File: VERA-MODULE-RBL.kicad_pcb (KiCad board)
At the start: 4 copper layers, 143 x 162.5 mm, 177 parts, among them J1 CONN_SMD_02x08_Odd_Even_2.54mm, J2 ICD15S13E4GX00LF, J3 CONN_DM3AT-SF-PEJM5, J4 DX07S016JA1R1500, J5 PJ-002AH-SMT-TR, Q1 MOSFET-BSS138-SOT-23, Q2 MOSFET-BSS138-SOT-23, Q3 BC817,SOT-23, Q4 BC817,SOT-23, Q5 MOSFET-BSS138-SOT-23, SW1 SPST2P, SW2 SPST_SWITCH_SMD_4P,4.1x5.4mm, U1 TXS0108EPW, U10 W25Q16JVSNIQ, U11 WM8524CGEDT, U12 USBCH340T, U13 AMS1117-3.3, U14 AMS1117-1.5, U15 L7805, U16 TXS0108EPW, U17 MAX40200AUK, U2 ICE40UP5K-SG48ITR, U3 TXS0108EPW, U4 TXS0108EPW, U5 IC74HC00, U6 TXS0108EPW, U7 ESP32-PICO-D4, U8 74CBTLV3126PW,118, U9 IC74HC00, X1 SG-5032CAN, Y1 12MHzC

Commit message: Updated
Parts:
- C11, C26, C27, C29, C32, C33, C35, R42, R6, R66, U16, U3, U8: moved to B.Cu
- C2, R2, R64, U1, U6: moved to F.Cu
- X1: value SG-5032CAN -> ECS-2033-250-BN; footprint Oscillator:Oscillator_SMD_SeikoEpson_SG8002LB-4Pin_5.0x3.2mm -> RetroBitLab:OSC_ECS-2033-250-BN
- moved C26 125.3 mm to (256.4, 50.5)
- moved R41 121.0 mm to (273.2, 72.2), turned to 90 degrees
- moved C28 118.4 mm to (259.4, 61.5), turned to 90 degrees
- moved C27 110.8 mm to (250.6, 50.9), turned to 180 degrees
- moved R37 110.7 mm to (263.2, 72.1), turned to 90 degrees
- moved C52 110.2 mm to (259.4, 56.2), turned to 270 degrees
- moved R39 108.1 mm to (268.1, 72.2), turned to 90 degrees
- moved R40 106.6 mm to (270.6, 72.2), turned to 90 degrees
- moved R49 102.8 mm to (165.8, 77.0), turned to 180 degrees
- moved R38 100.7 mm to (265.6, 72.1), turned to 90 degrees
- moved U8 97.8 mm to (250.4, 57.9), turned to 90 degrees
- moved C29 94.1 mm to (239.4, 54.0)
- moved R42 89.4 mm to (245.6, 54.9), turned to 180 degrees
- moved R44 88.5 mm to (235.4, 67.6), turned to 180 degrees
- moved C34 87.8 mm to (232.0, 84.9)
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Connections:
- C1 pad 2: +3V3 -> 3V3
- C10 pad 2: +5V -> 3V3
- C11 pad 2: +3V3 -> 3V3
- C12 pad 2: +5V -> 5V
- C2 pad 2: +5V -> 3V3
- C55 pad 2: +3V3 -> 5V
- C56 pad 2: +5V -> 5V
- C57 pad 2: +3V3 -> 5V
- C58 pad 2: +5V -> 5V
- C9 pad 2: +3V3 -> 3V3
- J2 pad 9: +5V -> 5V
- LD2 pad 2: +3V3 -> 3V3
- R2 pad 1: +3V3 -> 3V3
- R6 pad 1: +3V3 -> 3V3
- R64 pad 1: +3V3 -> 3V3
- R66 pad 1: +3V3 -> 3V3
- R7 pad 1: +3V3 -> 3V3
- U1 pad 1: mD2 -> mRD4
- U1 pad 12: ~S4 -> A12
- U1 pad 13: A3 -> A9
- U1 pad 14: A2 -> A8
- U1 pad 15: A1 -> A7
- U1 pad 16: A0 -> A6
- U1 pad 17: D4 -> A5
- U1 pad 18: D5 -> A4
- U1 pad 19: +5V -> 5V
- U1 pad 2: +3V3 -> 3V3
- U1 pad 20: D2 -> RD4
- U1 pad 3: mD5 -> mA4
- U1 pad 4: mD4 -> mA5
- U1 pad 5: mA0 -> mA6
- U1 pad 6: mA1 -> mA7
- U1 pad 7: mA2 -> mA8
- U1 pad 8: mA3 -> mA9
- U1 pad 9: ~mS4 -> mA12
- U16 pad 1: ~mHALT -> ~FPGA_RESET
- U16 pad 12: ~WE -> D1
- U16 pad 13: ~RE -> D0
- U16 pad 14: ~MPD -> D6
- U16 pad 15: ~D1XX -> ~S5
- U16 pad 16: A15 -> RD5
- U16 pad 17: A14 -> ~CCTL
- U16 pad 18: A13 -> ~EXSEL
- U16 pad 19: +5V -> 5V
- U16 pad 2: +3V3 -> 3V3
- U16 pad 20: ~HALT -> ~RST
- U16 pad 3: mA13 -> ~mEXSEL
- U16 pad 4: mA14 -> ~mCCTL
- U16 pad 5: mA15 -> mRD5
- U16 pad 6: ~mD1XX -> ~mS5
- U16 pad 7: ~mMPD -> mD6
- U16 pad 8: ~mRE -> mD0
- U16 pad 9: ~mWE -> mD1
- U3 pad 1: mRD4 -> mD2
- U3 pad 12: A12 -> ~S4
- U3 pad 13: A9 -> A3
- U3 pad 14: A8 -> A2
- U3 pad 15: A7 -> A1
- U3 pad 16: A6 -> A0
- U3 pad 17: A5 -> D4
- U3 pad 18: A4 -> D5
- U3 pad 19: +5V -> 5V
- U3 pad 2: +3V3 -> 3V3
- U3 pad 20: RD4 -> D2
- U3 pad 3: mA4 -> mD5
- U3 pad 4: mA5 -> mD4
- U3 pad 5: mA6 -> mA0
- U3 pad 6: mA7 -> mA1
- U3 pad 7: mA8 -> mA2
- U3 pad 8: mA9 -> mA3
- U3 pad 9: mA12 -> ~mS4
- U4 pad 1: mD3 -> ~mHALT
- U4 pad 12: ~IRQ -> ~WE
- U4 pad 13: RSRVD -> ~RE
- U4 pad 14: PHI2 -> ~MPD
- U4 pad 15: R~W -> ~D1XX
- U4 pad 16: A10 -> A15
- U4 pad 17: A11 -> A14
- U4 pad 18: D7 -> A13
- U4 pad 19: +5V -> 5V
- U4 pad 2: +3V3 -> 3V3
- U4 pad 20: D3 -> ~HALT
- U4 pad 3: mD7 -> mA13
- U4 pad 4: mA11 -> mA14
- U4 pad 5: mA10 -> mA15
- U4 pad 6: mR~W -> ~mD1XX
- U4 pad 7: mPHI2 -> ~mMPD
- U4 pad 8: mRSRVD -> ~mRE
- U4 pad 9: ~mVIRQ -> ~mWE
- U6 pad 1: ~FPGA_RESET -> mD3
- U6 pad 12: D1 -> ~IRQ
- U6 pad 13: D0 -> RSRVD
- U6 pad 14: D6 -> PHI2
- U6 pad 15: ~S5 -> R~W
- U6 pad 16: RD5 -> A10
- U6 pad 17: ~CCTL -> A11
- U6 pad 18: ~EXSEL -> D7
- U6 pad 19: +5V -> 5V
- U6 pad 2: +3V3 -> 3V3
- U6 pad 20: ~RST -> D3
- U6 pad 3: ~mEXSEL -> mD7
- U6 pad 4: ~mCCTL -> mA11
- U6 pad 5: mRD5 -> mA10
- U6 pad 6: ~mS5 -> mR~W
- U6 pad 7: mD6 -> mPHI2
- U6 pad 8: mD0 -> mRSRVD
- U6 pad 9: mD1 -> ~mVIRQ
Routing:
- net 5V: track 41.9 -> 617.0 mm, vias 3 -> 19
- net GND: track 93.6 -> 406.9 mm, vias 26 -> 92
- net 3V3: track 88.7 -> 399.5 mm, vias 14 -> 76
- net AUDIOL: track 2.23 -> 217.3 mm, vias 0 -> 3
- net ~mD1XX: track 0.00 -> 194.5 mm, vias 0 -> 11
- net ~D1XX: track 27.9 -> 217.7 mm, vias 2 -> 9
- net AUDIOR: track 2.09 -> 182.1 mm, vias 0 -> 6
- net TXB_EN: track 13.2 -> 191.9 mm, vias 0 -> 10
- net mD0: track 2.04 -> 180.8 mm, vias 1 -> 7
- net mA3: track 11.5 -> 181.3 mm, vias 0 -> 10
- net mA1: track 10.6 -> 178.3 mm, vias 0 -> 9
- net mD5: track 0.00 -> 161.0 mm, vias 0 -> 7
- net mD7: track 0.00 -> 160.7 mm, vias 0 -> 10
- net mD4: track 0.00 -> 160.5 mm, vias 0 -> 6
- net mA7: track 0.00 -> 159.5 mm, vias 0 -> 5
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- added copper zone on F.Cu, net 3V3
- added copper zone on POWER, net 3V3
- added copper zone on B.Cu, net GND
- added copper zone on F.Cu, net GND
- added copper zone on GND, net GND
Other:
- board text added: "EXTERNAL VIDEO CONNECTOR"
- board text added: "VERA READY"

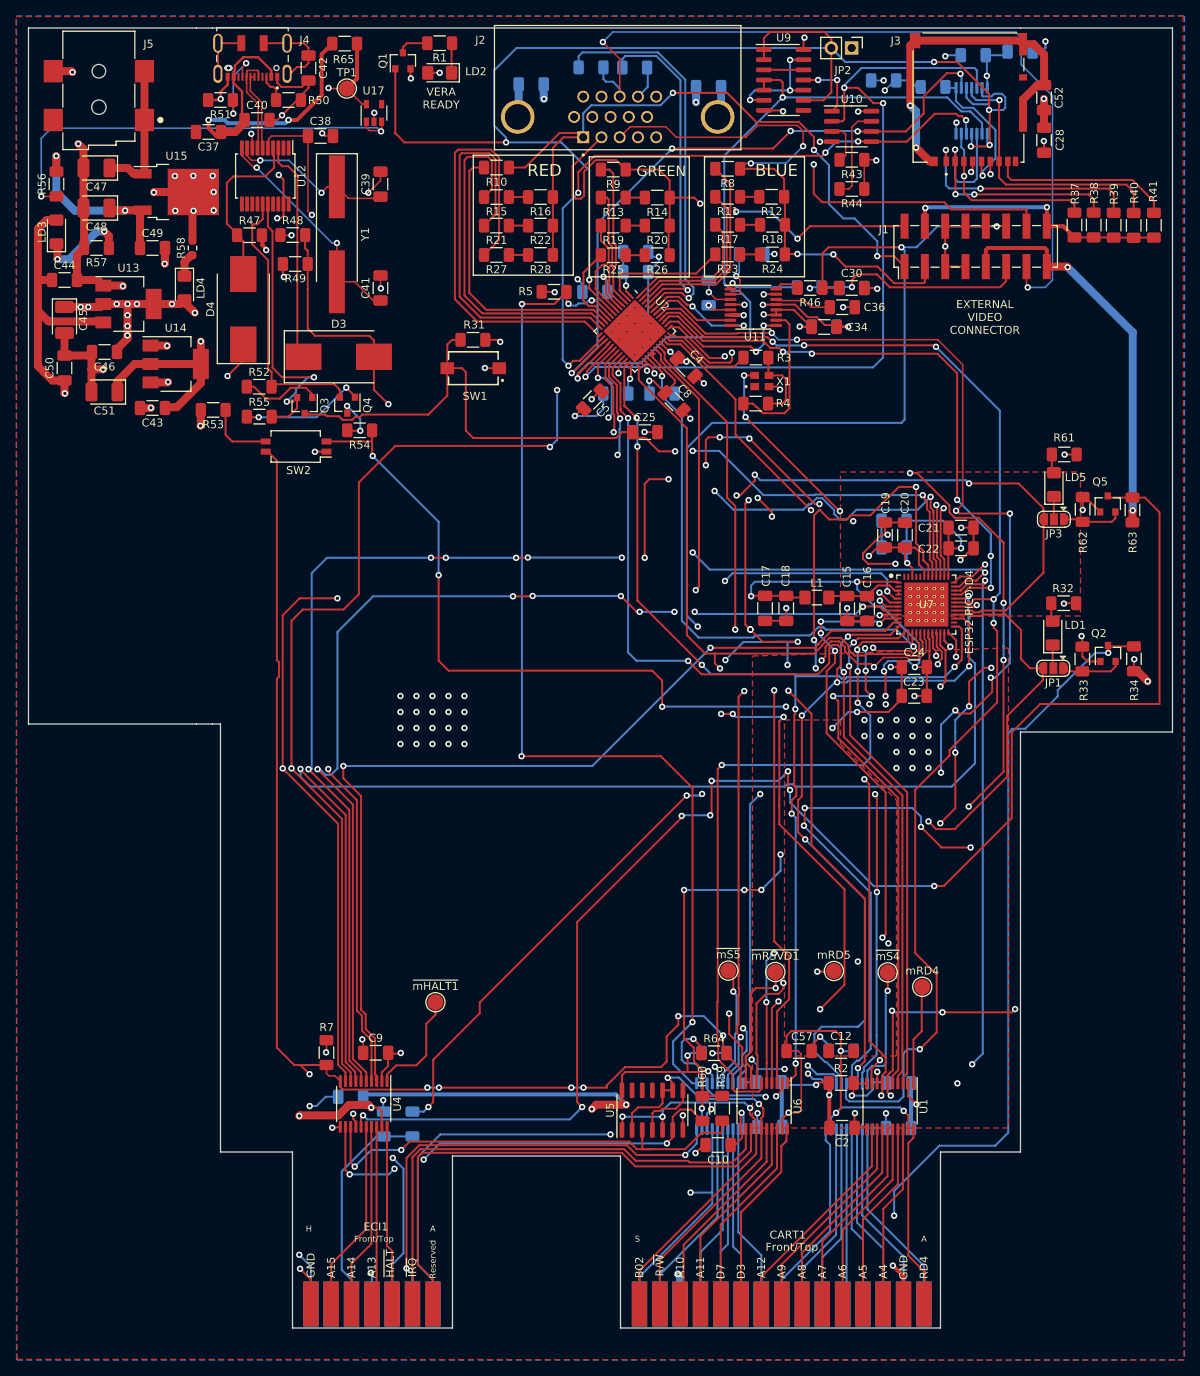
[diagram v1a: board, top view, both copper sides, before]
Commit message: Fiducials & Logo added
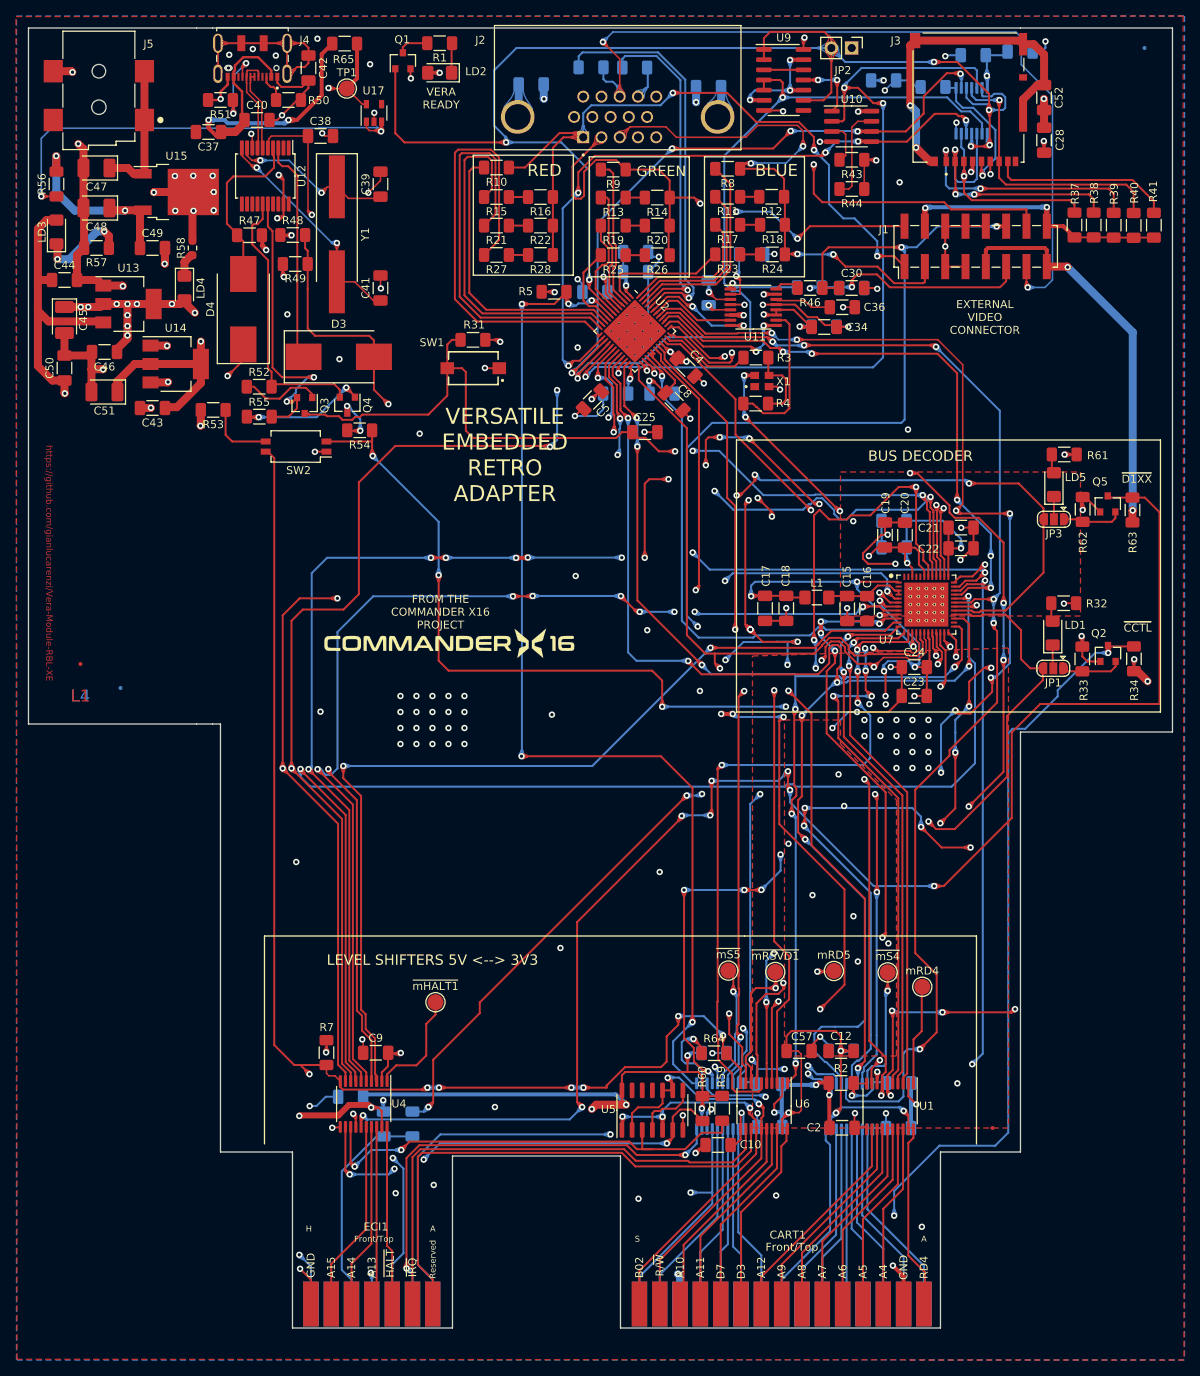
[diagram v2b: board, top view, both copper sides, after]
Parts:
- added FID1: Fiducial, Fiducial:Fiducial_0.5mm_Mask1mm, B.Cu at (272.0, 50.0)
- added FID2: Fiducial, Fiducial:Fiducial_0.5mm_Mask1mm, B.Cu at (144.0, 130.0)
- added FID3: Fiducial, Fiducial:Fiducial_0.5mm_Mask1mm, F.Cu at (139.0, 127.0)
- added FID4: Fiducial, Fiducial:Fiducial_0.5mm_Mask1mm, F.Cu at (253.0, 185.0)
- added LOGO1: VERA X16 LOGO, RetroBitLab:x16logo, F.Cu at (185.1, 124.4)
- moved R66 0.28 mm to (225.1, 179.5)
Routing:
- net GND: track 406.9 -> 427.8 mm, vias 92 -> 122
- net Net-(C42-Pad1): track 17.7 -> 24.4 mm
- net 5V: track 617.0 -> 618.6 mm
- net 3V3: track 399.5 -> 398.6 mm
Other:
- board text added: "BUS DECODER"
- board text added: "FROM THE COMMANDER X16 PROJECT"
- board text added: "L1"
- board text added: "L2"
- board text added: "L3"
- board text added: "L4"
- board text added: "LEVEL SHIFTERS 5V <--> 3V3"
- board text added: "VERSATILE EMBEDDED RETRO ADAPTER"
- board text added: "https://github.com/gianlucarenzi/Vera-Module-RBL-XE"
- board text added: "in memoriam A.S. - G.D."
- board text added: "~CCTL"
- board text added: "~D1XX"

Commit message: Update to more available components by LCSC
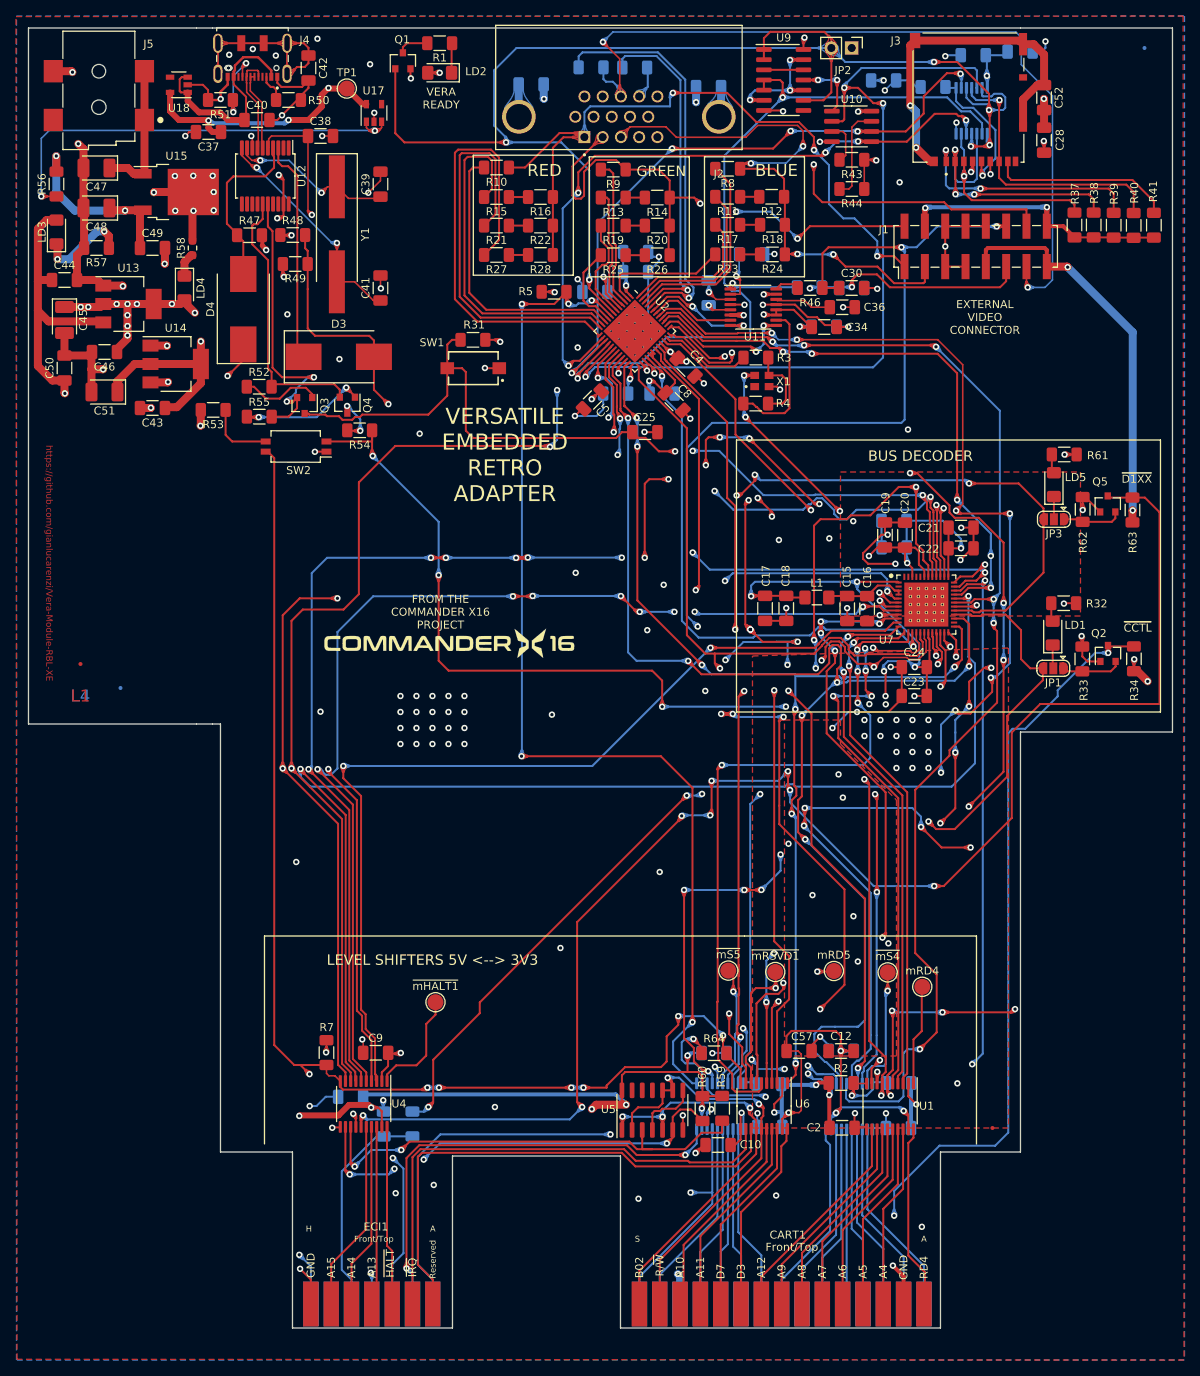
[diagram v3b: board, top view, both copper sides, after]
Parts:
- removed R65: 0R, Resistor_SMD:R_1206_3216Metric_Pad1.30x1.75mm_HandSolder
- added U18: MAX40200AUK, Package_TO_SOT_SMD:SOT-23-5, F.Cu at (151.3, 54.6)
- J2: value ICD15S13E4GX00LF -> XDDB-1518-0932
- J5: footprint RetroBitLab:CUI_PJ-002AH-SMT-TR -> CUI_PJ-002AH-SMT-TR
- moved J2 0.15 mm to (206.3, 58.6)
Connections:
- C37 pad 1: 5V_USB -> 5V
- C40 pad 1: 5V_USB -> Net-(C40-Pad1)
- J4 pad 11: 5V_USB -> Net-(C40-Pad1)
- J4 pad 2: 5V_USB -> Net-(C40-Pad1)
- R47 pad 2: 5V_USB -> 5V
- U12 pad 19: 5V_USB -> 5V
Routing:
- net 5V_USB: track 71.4 -> 0.00 mm, vias 5 -> 0
- net 5V: track 618.6 -> 668.3 mm, vias 19 -> 24
- net Net-(C40-Pad1): track 0.00 -> 27.2 mm
- net GND: track 427.8 -> 433.0 mm, vias 122 -> 126
- net mA2: track 150.4 -> 148.7 mm
- net Net-(R56-Pad1): track 56.4 -> 55.0 mm
- net /VeraModule/VGARED: track 87.1 -> 87.9 mm

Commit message: Update to more available components by LCSC Added another MAX20400 Schottky Diode protection for USB
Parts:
- J5: footprint CUI_PJ-002AH-SMT-TR -> RetroBitLab:CUI_PJ-002AH-SMT-TR
